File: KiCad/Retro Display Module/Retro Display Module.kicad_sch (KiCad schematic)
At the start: 0 parts

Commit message: Add: PCB
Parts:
- added C1, C3: 10pF, Capacitor_SMD:C_0402_1005Metric, symbol Device:C_Small
- added C2, C5, C7: 0.1uF, Capacitor_SMD:C_0402_1005Metric, symbol Device:C_Small
- added C4: 1nF, Capacitor_SMD:C_0805_2012Metric, symbol Device:C_Small
- added C6: 4.7uF, Capacitor_SMD:C_0402_1005Metric, symbol Device:C_Small
- added J1, J18, J19, J21: Conn_01x04_Pin, Connector_PinHeader_2.54mm:PinHeader_1x04_P2.54mm_Vertical, symbol Connector:Conn_01x04_Pin
- added J10, J11, J20, J8, J9: Conn_01x02_Pin, Connector_PinHeader_2.54mm:PinHeader_1x02_P2.54mm_Vertical, symbol Connector:Conn_01x02_Pin
- added J12, J2: VCC, Library:CONN-SMD_YZF0002-38080-02, symbol Connector_Generic:Conn_01x01
- added J13, J3: TX, Library:CONN-SMD_YZF0002-38080-02, symbol Connector_Generic:Conn_01x01
- added J14, J4: RX, Library:CONN-SMD_YZF0002-38080-02, symbol Connector_Generic:Conn_01x01
- added J15, J5: CFG, Library:CONN-SMD_YZF0002-38080-02, symbol Connector_Generic:Conn_01x01
- added J16, J6: SEL, Library:CONN-SMD_YZF0002-38080-02, symbol Connector_Generic:Conn_01x01
- added J17, J7: GND, Library:CONN-SMD_YZF0002-38080-02, symbol Connector_Generic:Conn_01x01
- added R1, R2, R6, R7, R8, R9: 4.7k, Resistor_SMD:R_0805_2012Metric, symbol Device:R_Small_US
- added R3, R4, R5: 10k, Resistor_SMD:R_0402_1005Metric, symbol Device:R_Small_US
- added U1: TS-1187A-B-A-B, Library:SW-SMD_4P-L5.1-W5.1-P3.70-LS6.5-TL-2, symbol EEE4022S:TS-1187A-B-A-B
- added U2: STM32G030C8T6, Library:LQFP-48_L7.0-W7.0-P0.50-LS9.0-BL_1, symbol EEE4022S:STM32G030C8T6
- added U3: AO3401A, Library:SOT-23_L2.9-W1.3-P1.90-LS2.4-BR, symbol EEE4022S:AO3401A
- added Y1: Crystal, Library:CRYSTAL-SMD_L11.5-W4.8-LS12.7, symbol Device:Crystal
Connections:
- new net: C4.1, J10.2 (Pin_2), R1.1
- new net: J19.2 (Pin_2), R4.1, R5.1
- new net: J20.1 (Pin_1), R6.1, R7.1, R8.1, R9.1
- new net: J10.1 (Pin_1), J14.1 (Pin_1), J4.1 (Pin_1), U3.3 (D)
- new net: J15.1 (Pin_1), J5.1 (Pin_1)
- new net: J6.1 (Pin_1), J8.1 (Pin_1)
- new net: C1.1, U2.8 (PF0-OSC_IN), Y1.1
- new net: J1.1 (Pin_1), U2.38 (PD0)
- new net: J1.2 (Pin_2), U2.39 (PD1)
- new net: J1.3 (Pin_3), U2.40 (PD2)
- new net: J1.4 (Pin_4), U2.41 (PD3)
- new net: J16.1 (Pin_1), R2.1, U3.1 (G)
- new net: C3.1, U2.9 (PF1-OSC_OUT), Y1.2
- new net: J18.2 (Pin_2), U2.35 (PA13)
- new net: J18.3 (Pin_3), U2.36 (PA14-BOOT0)
- new net: J18.4 (Pin_4), R3.2
- new net 3V3: J19.1 (Pin_1), J8.2 (Pin_2), J9.1 (Pin_1)
- new net 5V: J20.2 (Pin_2)
- new net GND: C1.2, C2.2, C3.2, C4.2, C5.2, C6.2, C7.2, J17.1 (Pin_1), J7.1 (Pin_1), R1.2, R2.2, R3.1, U1.3 (C), U1.4 (D), U2.7 (VSSA/SSA)
- new net I2C1_SCL: J19.3 (Pin_3), R5.2, U2.45 (PB6)
- new net I2C1_SDA: J19.4 (Pin_4), R4.2, U2.46 (PB7)
- new net NRST: C2.1, J18.1 (Pin_1), U1.1 (A), U1.2 (B), U2.10 (NRST)
- new net PA4: U2.15 (PA4)
- new net PA5: U2.16 (PA5)
- new net PA6: U2.17 (PA6)
- new net PA7: U2.18 (PA7)
- new net PB10: U2.22 (PB10)
- new net PB11: U2.23 (PB11)
- new net PB12: U2.24 (PB12)
- new net PB13: U2.25 (PB13)
- new net PB14: U2.26 (PB14)
- new net PB2: U2.21 (PB2)
- new net PB8: U2.47 (PB8)
- new net PB9: U2.48 (PB9)
- new net TIM1_CH1: U2.28 (PA8)
- new net TIM1_CH2: U2.29 (PA9)
- new net TIM3_CH1: J21.1 (Pin_1), R6.2, U2.43 (PB4)
- new net TIM3_CH2: J21.2 (Pin_2), R7.2, U2.44 (PB5)
- new net TIM3_CH3: J21.3 (Pin_3), R8.2, U2.19 (PB0)
- new net TIM3_CH4: J21.4 (Pin_4), R9.2, U2.20 (PB1)
- new net USART2_Rx: J11.1 (Pin_1), J3.1 (Pin_1), U2.14 (PA3)
- new net USART2_Tx: J11.2 (Pin_2), J13.1 (Pin_1), U2.13 (PA2), U3.2 (S)
- new net VCC: J12.1 (Pin_1), J2.1 (Pin_1)
- new net VR/B: C5.1, C6.1, C7.1, J9.2 (Pin_2), U2.4 (VBAT), U2.5 (VREF+), U2.6 (VDDA/DDA)
- no-connect marks 0 -> 13
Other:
- added sheet LED Driver (LED Driver.kicad_sch)
- added sheet Power (Power.kicad_sch)
- added sheet RGB LEDs (RGB_LEDs.kicad_sch)
- note added: "Pogo Pins"
- note added: "Pogo Targets"

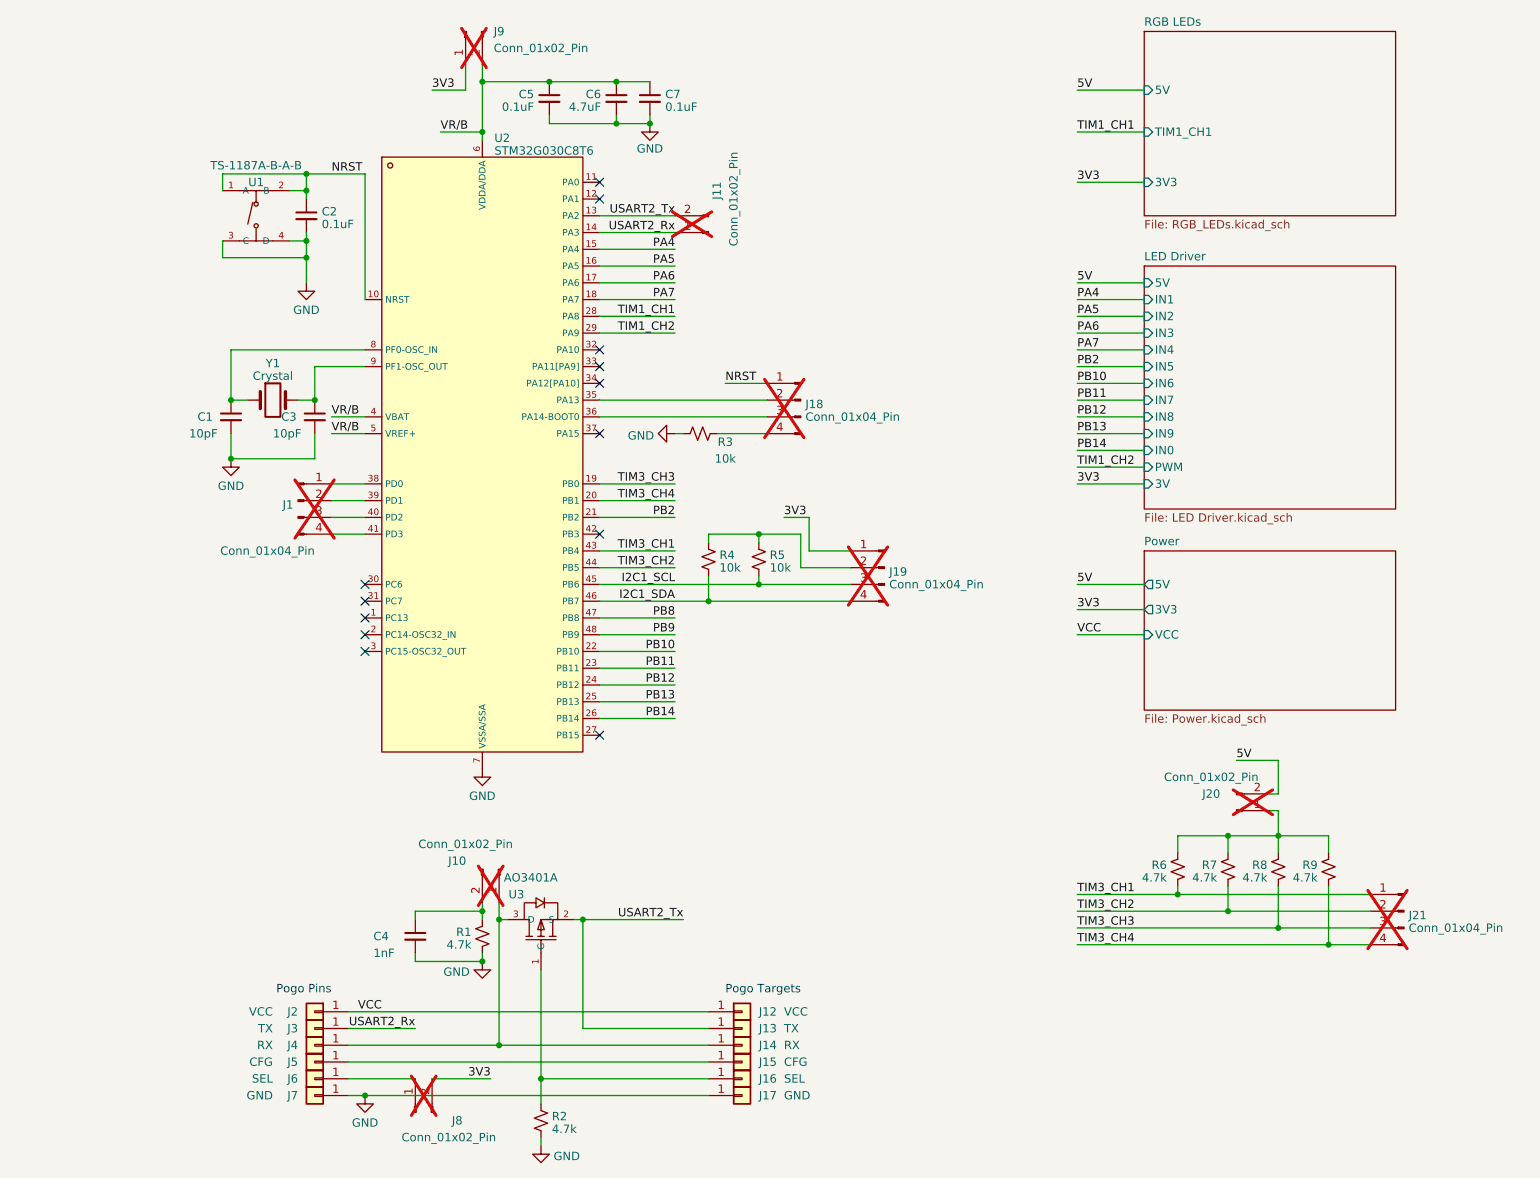
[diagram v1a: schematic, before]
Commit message: Updated USB PD and Driver LED circuit
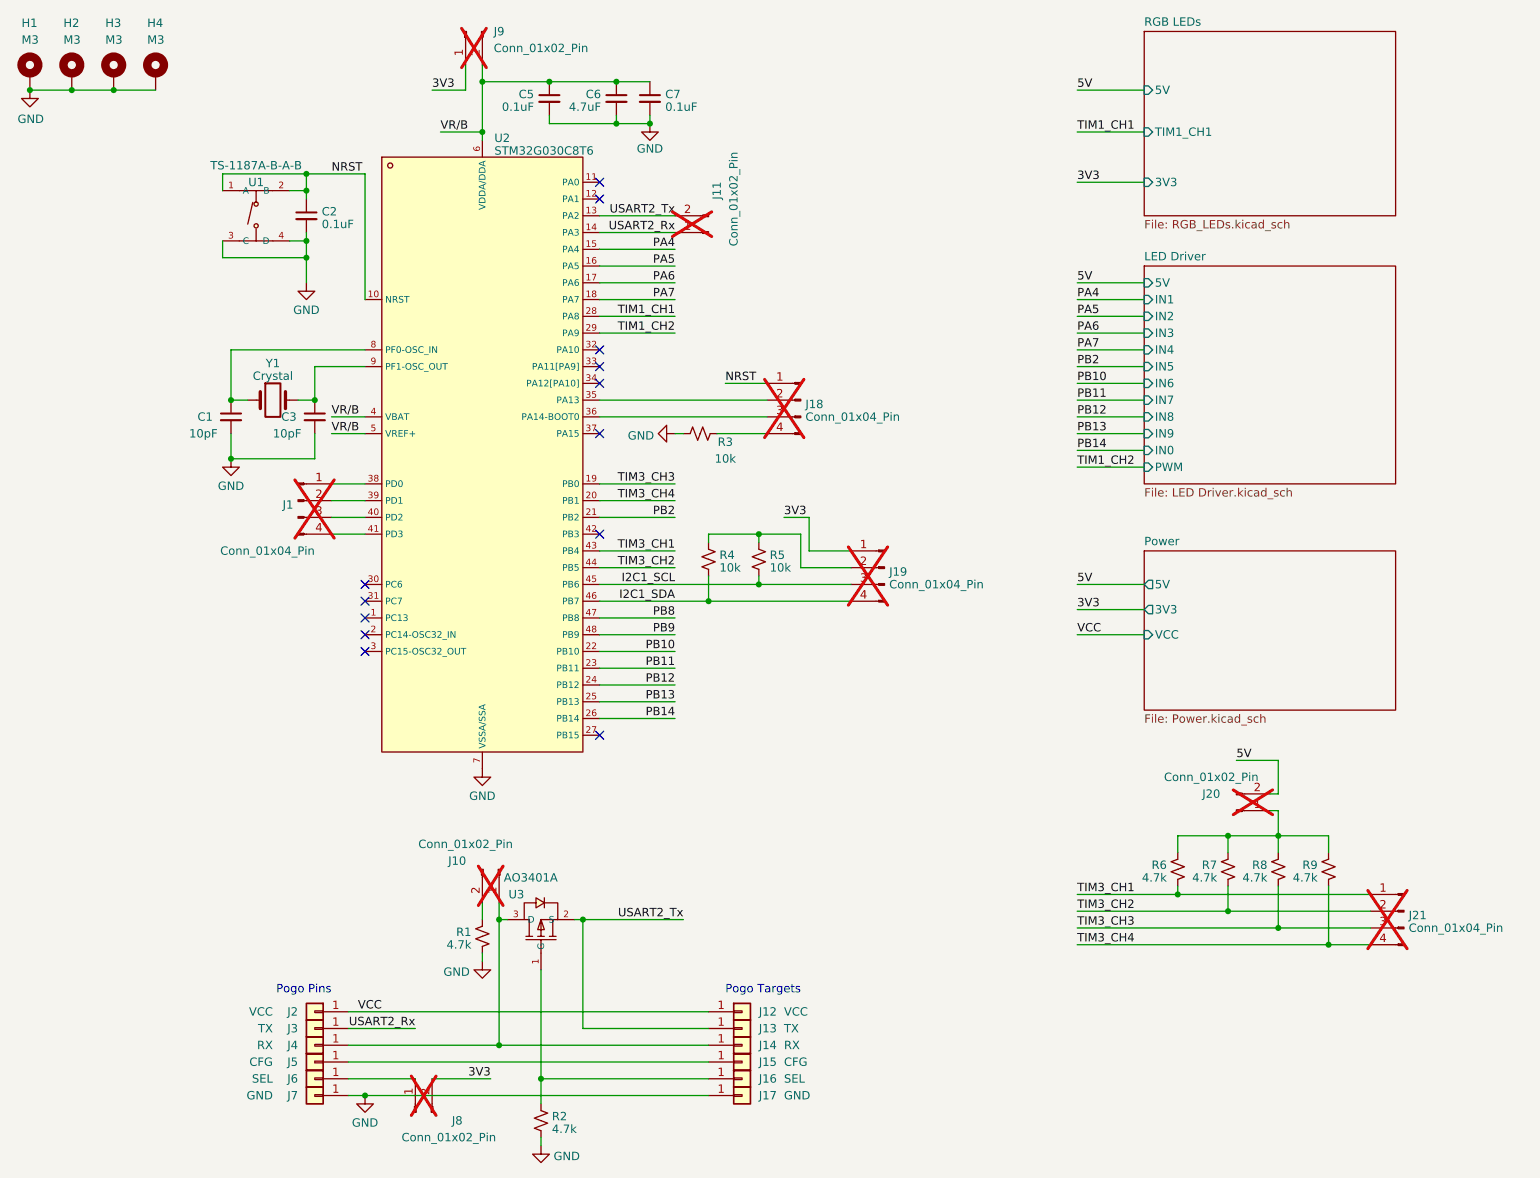
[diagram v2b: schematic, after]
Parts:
- removed C4: 1nF, Capacitor_SMD:C_0805_2012Metric, symbol Device:C_Small
- added H1, H2, H3, H4: M3, Library:MountingHole_3.2mm_M3_Pad_TopBottom, symbol Mechanical:MountingHole_Pad
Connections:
- net GND: now also H1.1, H2.1, H3.1, H4.1
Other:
- sheet LED Driver ports: added none; removed 3V

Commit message: Updated Display Board schematic and Ltspice simulations
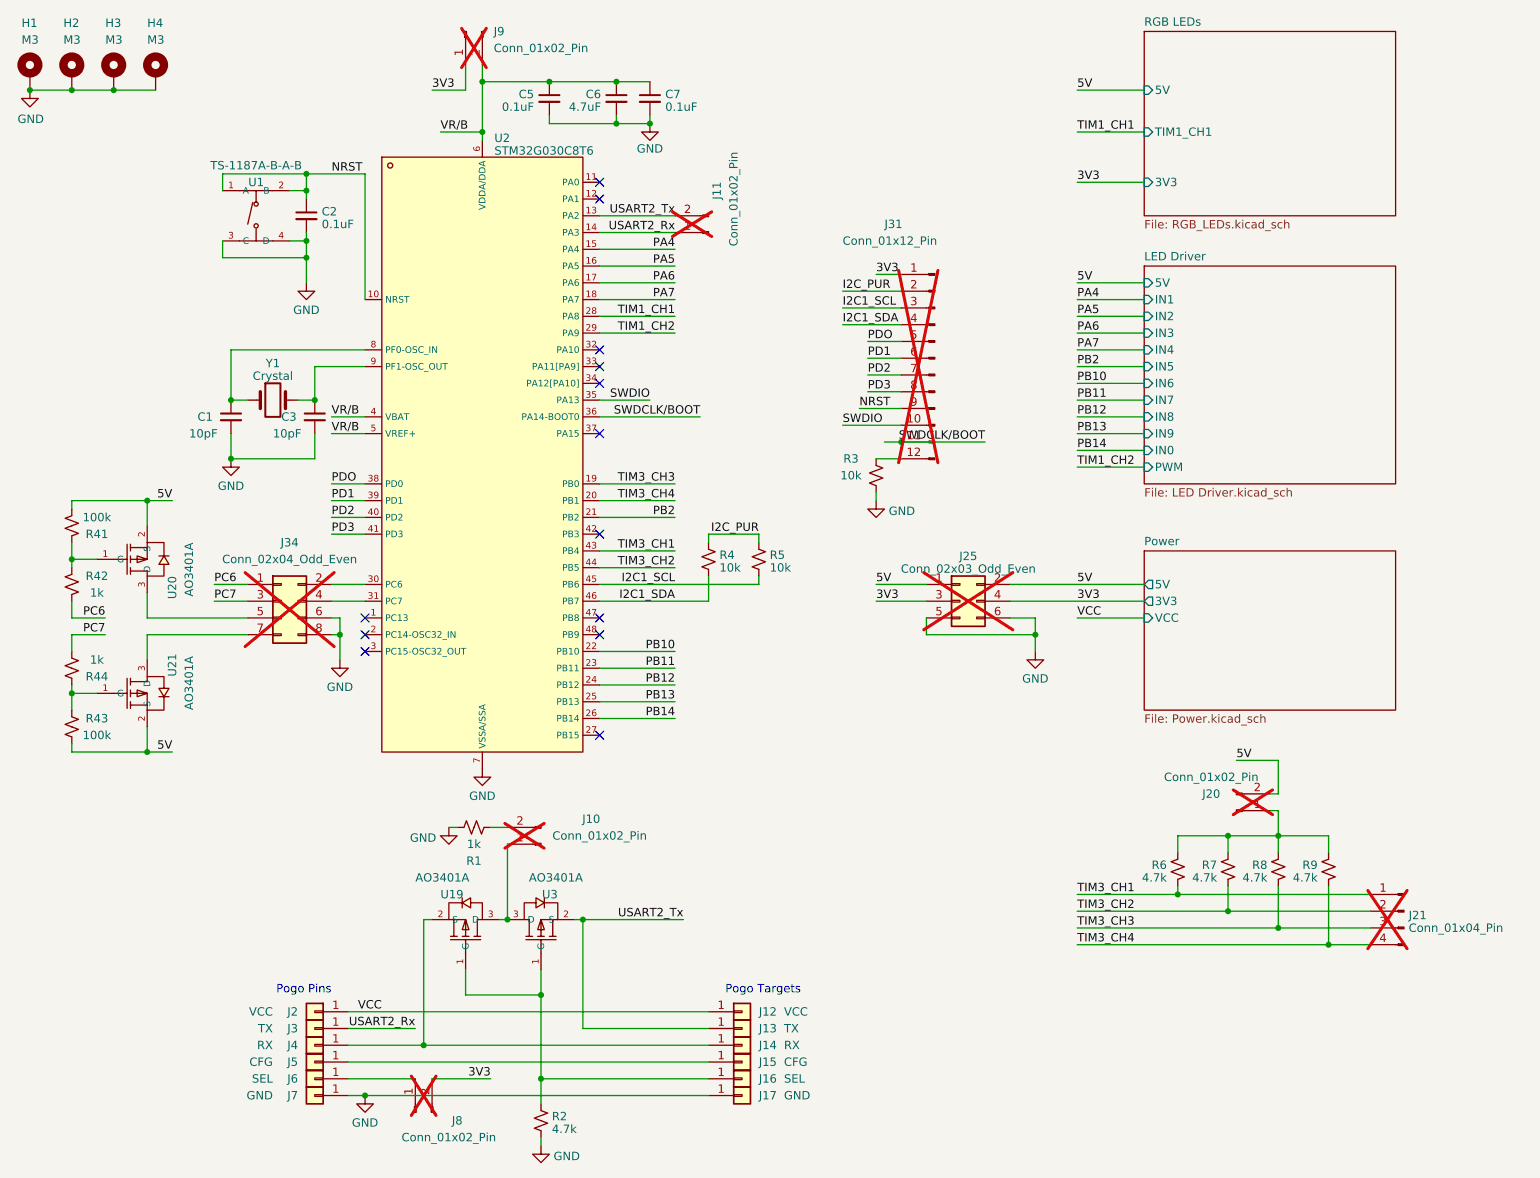
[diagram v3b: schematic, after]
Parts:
- removed J1, J18, J19: Conn_01x04_Pin, Connector_PinHeader_2.54mm:PinHeader_1x04_P2.54mm_Vertical, symbol Connector:Conn_01x04_Pin
- added J25: Conn_02x03_Odd_Even, Connector_PinHeader_2.54mm:PinHeader_2x03_P2.54mm_Vertical, symbol Connector_Generic:Conn_02x03_Odd_Even
- added J31: Conn_01x12_Pin, Connector_PinHeader_2.54mm:PinHeader_1x12_P2.54mm_Vertical, symbol Connector:Conn_01x12_Pin
- added J34: Conn_02x04_Odd_Even, Connector_PinHeader_2.54mm:PinHeader_2x04_P2.54mm_Vertical, symbol Connector_Generic:Conn_02x04_Odd_Even
- added R41, R43: 100k, Resistor_SMD:R_0402_1005Metric, symbol Device:R_Small_US
- added R42, R44: 1k, Resistor_SMD:R_0402_1005Metric, symbol Device:R_Small_US
- added U19, U20, U21: AO3401A, Library:SOT-23_L2.9-W1.3-P1.90-LS2.4-BR, symbol EEE4022S:AO3401A
- R1: value 4.7k -> 1k; LCSC C17673 -> C17513
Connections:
- net 3V3: now also J25.3 (Pin_3), J25.4 (Pin_4), J31.1 (Pin_1)
- net 5V: now also J25.1 (Pin_1), J25.2 (Pin_2), R41.1, R43.1, U20.2 (S), U21.2 (S)
- net GND: now also J25.5 (Pin_5), J25.6 (Pin_6), J34.6 (Pin_6), J34.8 (Pin_8)
- net I2C1_SCL: now also J31.3 (Pin_3)
- net I2C1_SDA: now also J31.4 (Pin_4)
- net NRST: now also J31.9 (Pin_9)
- net I2C_PUR: now reaches R4.1, R5.1
- net I2C_PUR: now also J31.2 (Pin_2)
- net at J14.1 (Pin_1), J4.1 (Pin_1): now also U19.2 (S); no longer J10.1 (Pin_1), U3.3 (D)
- net PDO: now reaches U2.38 (PD0)
- net PDO: now also J31.5 (Pin_5)
- net PD1: now reaches U2.39 (PD1)
- net PD1: now also J31.6 (Pin_6)
- net PD2: now reaches U2.40 (PD2)
- net PD2: now also J31.7 (Pin_7)
- net PD3: now reaches U2.41 (PD3)
- net PD3: now also J31.8 (Pin_8)
- net at J16.1 (Pin_1), R2.1, U3.1 (G): now also U19.1 (G)
- net at U2.30 (PC6): now also J34.2 (Pin_2)
- net at U2.31 (PC7): now also J34.4 (Pin_4)
- net SWDIO: now reaches U2.35 (PA13)
- net SWDIO: now also J31.10 (Pin_10)
- net SWDCLK/BOOT: now reaches U2.36 (PA14-BOOT0)
- net SWDCLK/BOOT: now also J31.11 (Pin_11)
- net at R3.2: now also J31.12 (Pin_12)
- net PB8: no longer names the net of U2.47 (PB8)
- net PB9: no longer names the net of U2.48 (PB9)
- new net: R43.2, R44.1, U21.1 (G)
- new net: R41.2, R42.1, U20.1 (G)
- new net: J34.5 (Pin_5), U20.3 (D)
- new net: J10.1 (Pin_1), U19.3 (D), U3.3 (D)
- new net: J34.7 (Pin_7), U21.3 (D)
- new net PC6: J34.1 (Pin_1), R42.2
- new net PC7: J34.3 (Pin_3), R44.2
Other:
- moved on the sheet: R3

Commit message: Updated Display PCB
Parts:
- renumbered C5 to C4, C6 to C5, C7 to C6, J31 to J18, R41 to R1, R6 to R10, R7 to R11, R8 to R12, R9 to R13, R42 to R2, R44 to R3, R43 to R4, R1 to R5, R2 to R6, R4 to R7, R5 to R8, R3 to R9, U20 to U1, U21 to U2, U1 to U3, U19 to U4, U2 to U5, U3 to U6
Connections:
- net GND: now also J34.4 (Pin_4); no longer J34.6 (Pin_6)
- net NRST: now also J18.11 (Pin_11); no longer J18.9 (Pin_9)
- net PC6: now also J34.5 (Pin_5); no longer J34.1 (Pin_1)
- net PC7: now also J34.1 (Pin_1); no longer J34.3 (Pin_3)
- net PD1: now also J18.7 (Pin_7); no longer J18.6 (Pin_6)
- net PD2: now also J18.6 (Pin_6); no longer J18.7 (Pin_7)
- net PD3: now also J18.5 (Pin_5); no longer J18.8 (Pin_8)
- net PDO: now also J18.8 (Pin_8); no longer J18.5 (Pin_5)
- net SWDCLK/BOOT: now also J18.9 (Pin_9); no longer J18.11 (Pin_11)
- net PA1: now reaches J15.1 (Pin_1), J5.1 (Pin_1)
- net PA1: now also U5.12 (PA1)
- net at U1.3 (D): now also J34.7 (Pin_7); no longer J34.5 (Pin_5)
- net at J34.2 (Pin_2): now also U5.31 (PC7); no longer U5.30 (PC6)
- net at U2.3 (D): now also J34.3 (Pin_3); no longer J34.7 (Pin_7)
- new net: J34.6 (Pin_6), U5.30 (PC6)
- no-connect marks 13 -> 12
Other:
- moved on the sheet: J34, R1, R2, R3, R4, R9, U1, U2

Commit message: Updated Display PCB
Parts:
- C1, C2, C3, C4, C5, C6: footprint Capacitor_SMD:C_0402_1005Metric -> Library:C_0402_1005Metric
- R1, R2, R3, R4, R7, R8, R9: footprint Resistor_SMD:R_0402_1005Metric -> Library:R_0402_1005Metric
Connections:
- net GND: now also J34.1 (Pin_1), J34.5 (Pin_5); no longer J34.4 (Pin_4), J34.8 (Pin_8)
- net PC6: now also J34.8 (Pin_8); no longer J34.5 (Pin_5)
- net PC7: now also J34.4 (Pin_4); no longer J34.1 (Pin_1)
- net at U1.3 (D): now also J34.6 (Pin_6); no longer J34.7 (Pin_7)
- net at J34.2 (Pin_2): now also U2.3 (D); no longer U5.31 (PC7)
- net at J34.3 (Pin_3): now also U5.31 (PC7); no longer U2.3 (D)
- net at U5.30 (PC6): now also J34.7 (Pin_7); no longer J34.6 (Pin_6)
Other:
- moved on the sheet: J34, R1, R2, R3, R4, U1, U2
